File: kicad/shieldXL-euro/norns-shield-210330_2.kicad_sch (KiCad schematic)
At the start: 48 parts, among them J1 PJ-320B, J2 PJ-320B, SW1 PVA1, SW2 PVA1, SW3 PVA1, U5 HCPL-0631-500E

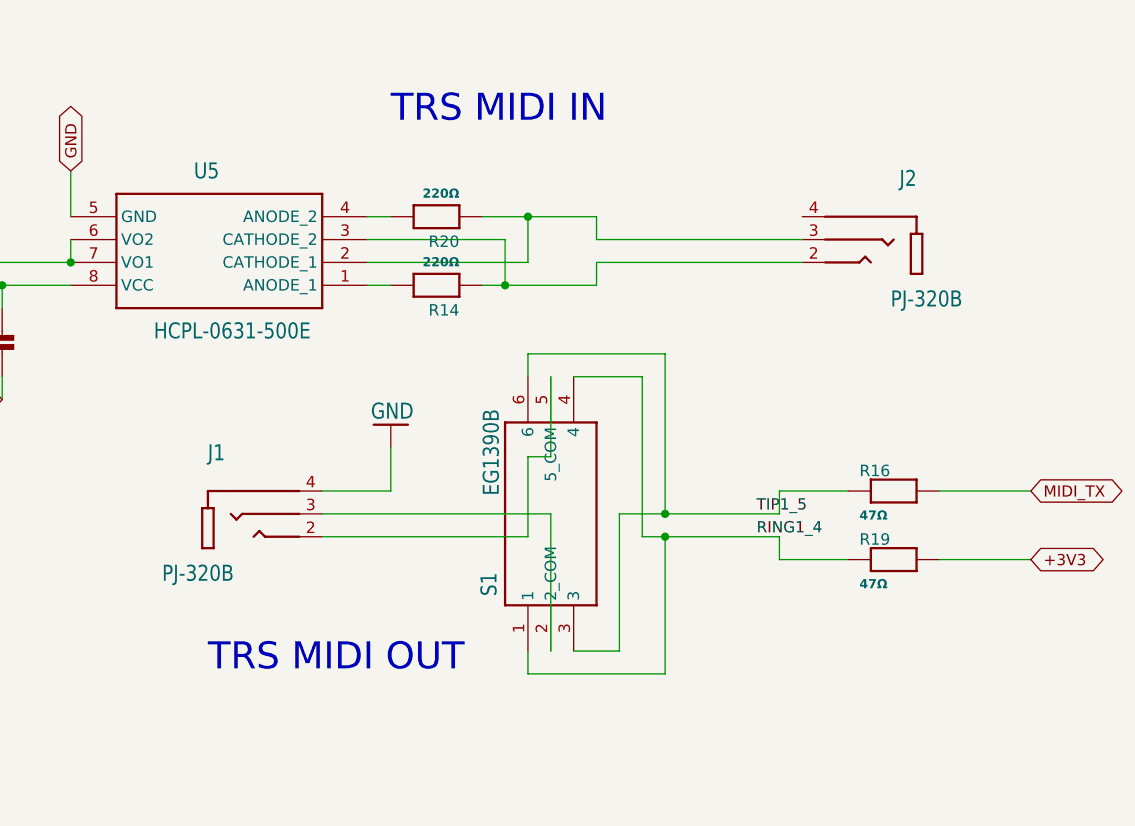
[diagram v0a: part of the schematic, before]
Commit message: Remove the desktop I/O: 6.35 mm jacks, PJ-320B MIDI jacks, A/B slide switch
tools/strip_shield_io.py takes J1, J2, J4, J5 off sheet 1 and J3, J6, S1 off
sheet 2, puts a global label wherever a signal reached them (IN_L_LINE,
IN_R_LINE, OUT_L_LINE, OUT_R_LINE, MIDI_OUT_SRC, MIDI_OUT_SNK, MIDI_IN_TIP,
MIDI_IN_RING), and prunes the wires left hanging. Checked against the
baseline netlist: every net keeps exactly its connections, less the removed
parts' pins. The Eurorack I/O that replaces them comes next.

Co-Authored-By: Claude Opus 5.5 <noreply@anthropic.com>
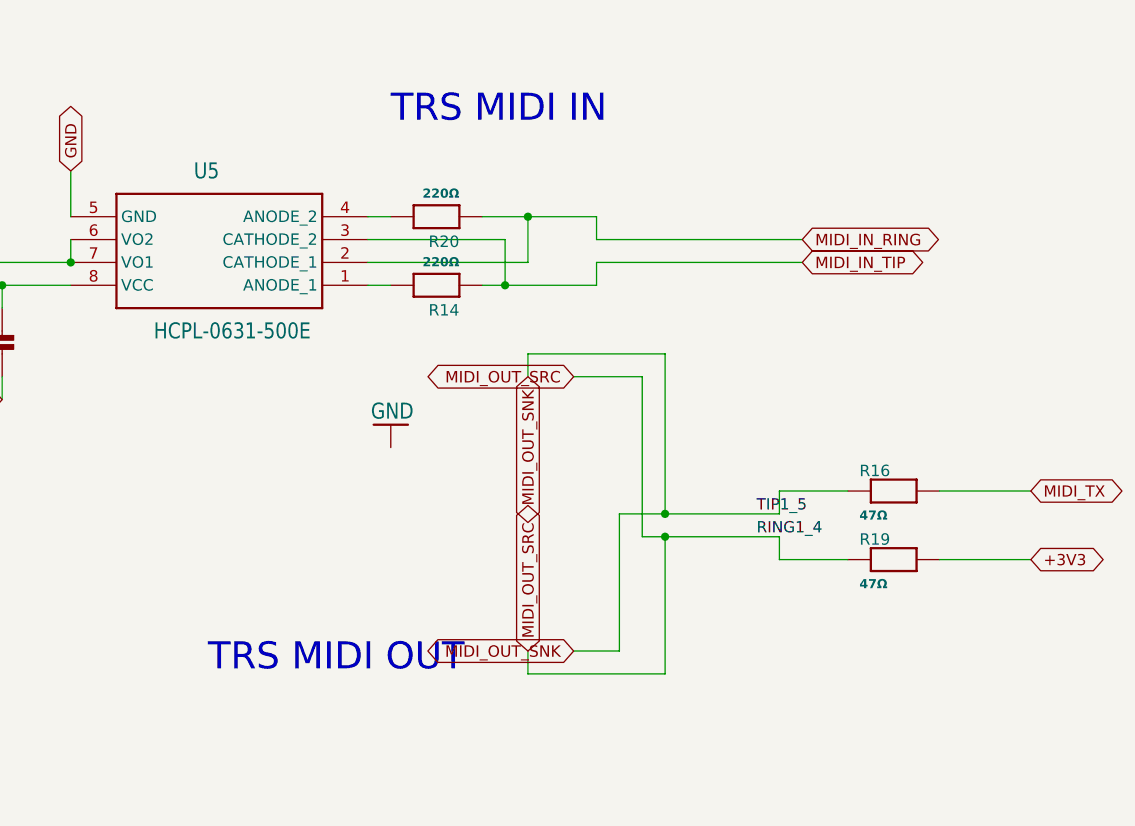
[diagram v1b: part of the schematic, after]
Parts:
- removed J1, J2: PJ-320B, ShieldXL:LUOYANG-DISHANG_PJ-320B, symbol Hachi-Ni_v26-eagle-import:PJ-320B
- removed S1: EG1390B, ShieldXL:SOP250P600X400-6N, symbol Hachi-Ni_v26-eagle-import:EG1390B
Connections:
- net MIDI_IN_RING: now reaches R20.1, U5.2 (CATHODE_1)
- net MIDI_IN_TIP: now reaches R14.1, U5.3 (CATHODE_2)
- net RING1_4 renamed MIDI_OUT_SRC
- net TIP1_5 renamed MIDI_OUT_SNK

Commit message: Add the Eurorack I/O sheet and the MMM footprint library
tools/make_eurorack_sheet.py writes eurorack.kicad_sch and hooks it into the
root as page 3: 10-pin rack power (op-amps only), 3.5 mm audio in/out through
a TL074 scaling 10 Vpp to the codec and back, PJ366ST MIDI jacks with Type A/B
on solder jumpers, USB-C power for the Pi through a polyfuse and TVS, and three
panel USB-A sockets cabled to the Pi. It joins the shield sheets by the global
labels the strip step placed.

strip_shield_io.py also removes the ground symbols left pinned to nothing once
the jacks were gone, in the same run as the strip. MMM.pretty and its 3D models
come from the Missing Mile Modular library; README.md covers the conversion,
the levels and what is left. Stop tracking __pycache__.

Co-Authored-By: Claude Opus 5.5 <noreply@anthropic.com>
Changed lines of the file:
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@@
-	)
-	(symbol
-		(lib_id "Hachi-Ni_v26-eagle-import:supply1_GND")
-		(at 196.85 53.594 180)
-		(unit 1)
-		(exclude_from_sim no)
-		(in_bom yes)
-		(on_board yes)
-		(dnp no)
-		(property "Reference" "#GND3"
-			(at 196.85 53.594 0)
-			(effects
-				(font
-					(size 1.27 1.27)
-				)
-				(hide yes)
-			)
-		)
-		(property "Value" "GND"
-			(at 199.39 51.054 0)
-			(effects
-				(font
-					(size 1.778 1.5113)
-				)
-				(justify left bottom)
-			)
-		)
-		(property "Footprint" ""
-			(at 196.85 53.594 0)
-			(effects
-				(font
-					(size 1.27 1.27)
-				)
-				(hide yes)
-			)
-		)
-		(property "Datasheet" ""
-			(at 196.85 53.594 0)
-			(effects
-				(font
-					(size 1.27 1.27)
-				)
-				(hide yes)
-			)
-		)
-		(property "Description" ""
-			(at 196.85 53.594 0)
-			(effects
-				(font
-					(size 1.27 1.27)
-				)
-				(hide yes)
-			)
-		)
-		(pin "1"
-		)
-		(instances
-			(project "Hachi-Ni_v26"
-				(path "/62ca0448-8214-4fa6-89ca-4a62b295d057/dcf1a22e-2574-4c83-a4dc-208deeeb6342"
-					(reference "#GND3")
-					(unit 1)
-				)
-			)
-			(project "shieldXL-euro"
-				(path "/b86e8947-58dc-49c6-bb5d-ce6d33c2e465/53fda09e-7af9-4285-ac8e-05ed312a27ba"
-					(reference "#GND06")
-					(unit 1)
-				)
-			)
-		)
 	)
 	(symbol

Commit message: Keys: C&K D6R00 round key switches for K1-K3
Footprint from the ITT Cannon D6 datasheet (D-18): four 0.8 mm PC pins on a
5.0 mm square, body d12.0, cap d9.0. The datasheet does not say which pins
pair inside, so SW1 and SW2 take opposite corners, on different contacts
either way; the other two pins hold the switch. Replaces shieldXL's
Choc/MX footprint, too wide for the 13.6 mm between K2 and K3.

Co-Authored-By: Claude Opus 5.5 <noreply@anthropic.com>
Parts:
- SW1, SW2, SW3: value PVA1 -> D6R00 F1 LFS; footprint ShieldXL:Choc_MX_combo -> MMM:SW_CK_D6R
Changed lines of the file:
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@@
 			)
 		)
-		(property "Value" "PVA1"
+		(property "Value" "D6R00 F1 LFS"
 			(at 240.03 198.12 0)
 			(effects
@@
 			)
 		)
-		(property "Footprint" "ShieldXL:Choc_MX_combo"
+		(property "Footprint" "MMM:SW_CK_D6R"
 			(at 243.84 196.85 0)
 			(effects
@@
 			)
 		)
-		(property "Value" "PVA1"
+		(property "Value" "D6R00 F1 LFS"
 			(at 240.03 165.1 0)
 			(effects
@@
 			)
 		)
-		(property "Footprint" "ShieldXL:Choc_MX_combo"
+		(property "Footprint" "MMM:SW_CK_D6R"
 			(at 243.84 163.83 0)
 			(effects
@@
 			)
 		)
-		(property "Value" "PVA1"
+		(property "Value" "D6R00 F1 LFS"
 			(at 240.03 129.54 0)
 			(effects
@@
 			)
 		)
-		(property "Footprint" "ShieldXL:Choc_MX_combo"
+		(property "Footprint" "MMM:SW_CK_D6R"
 			(at 243.84 128.27 0)
 			(effects

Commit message: Board: K1-K3 on the D6R footprint; keys are populated
shieldXL left its keys unfitted (DNP) for builders to choose; Moirae fits
the D6R00.

Co-Authored-By: Claude Opus 5.5 <noreply@anthropic.com>
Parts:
- SW1, SW2, SW3: now fitted
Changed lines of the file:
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@@
 		(in_bom yes)
 		(on_board yes)
-		(dnp yes)
+		(dnp no)
 		(property "Reference" "SW3"
 			(at 240.03 186.69 0)
@@
 		(in_bom yes)
 		(on_board yes)
-		(dnp yes)
+		(dnp no)
 		(property "Reference" "SW2"
 			(at 240.03 153.67 0)
@@
 		(in_bom yes)
 		(on_board yes)
-		(dnp yes)
+		(dnp no)
 		(property "Reference" "SW1"
 			(at 240.03 118.11 0)

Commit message: 3D models for shieldXL's parts; encoders populated
tools/set_3d_models.py gives the Eagle-imported footprints KiCad's stock
models, turned to match their pads (found by matching pad positions; KiCad
turns a model the opposite way to a footprint, checked on U1's pin 1), points
the encoders at the repo's PEC11R model instead of a missing Mac path, fixes
U2's KiCad 6 path, and stands the 1812 resistor model in for the fuse. Q1
takes the XO53 oscillator body (5.0 x 3.2, as the ASFL1).

E1-E3 were do-not-populate from shieldXL, which hid them in 3D; Moirae fits
them.

Co-Authored-By: Claude Opus 5.5 <noreply@anthropic.com>
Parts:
- E1, E2, E3: now fitted
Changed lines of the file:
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@@
 		(in_bom yes)
 		(on_board yes)
-		(dnp yes)
+		(dnp no)
 		(property "Reference" "E1"
 			(at 101.6 127 0)
@@
 		(in_bom yes)
 		(on_board yes)
-		(dnp yes)
+		(dnp no)
 		(property "Reference" "E2"
 			(at 101.6 177.8 0)
@@
 		(in_bom yes)
 		(on_board yes)
-		(dnp yes)
+		(dnp no)
 		(property "Reference" "E3"
 			(at 101.6 228.6 0)

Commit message: Circuit review: USB ESD and bulk, MIDI out buffer, panel MIDI LEDs, non-inverting inputs, display decoupling, AGND-GND jumper
- U102-U104 USBLC6-2SC6 on each panel USB-A's D+/D-, with 47u + 100n on
  its VBUS (C114-C119): the ports are on the panel, the Pi 10 cm away.
- U105 74LVC1G125 between the Pi's TXD and the MIDI out resistor and TX LED
  (MIDI_TX -> MIDI_TX_BUF): a TRS plug going in shorts tip/ring to sleeve,
  and the buffer takes that, not the Pi. R17 47 -> 100 ohm keeps that
  short under the buffer's 50 mA and the loop at about 5 mA.
- D1 / D2 come out to the panel: red 3 mm LEDs (MMM:LED_3mm_PadsAC, pads
  named A/C for shieldXL's symbol) between the MIDI jacks, 470 ohm each.
- Inputs: 69.8k / 30.1k divider into a follower instead of the inverting
  stage, so audio keeps its polarity; 13.4 Vpp reaches codec full scale.
- C121 / C122 10u + 100n on +3V3 at the display's FPC connector.
- JP103, open, across the AGND-GND ferrite L3.

Co-Authored-By: Claude Opus 5.5 <noreply@anthropic.com>
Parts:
- D6: value RED -> RED 3mm; footprint ShieldXL:CHIPLED_0603_NOOUTLINE -> MMM:LED_3mm_PadsAC
- D7: value BLUE -> RED 3mm; footprint ShieldXL:CHIPLED_0603_NOOUTLINE -> MMM:LED_3mm_PadsAC
- R16: value 47Ω -> 100Ω
- R21: value 47Ω -> 470Ω
- R22: value 15Ω -> 470Ω
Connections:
- net MIDI_TX renamed MIDI_TX_BUF
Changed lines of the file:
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@@
 		)
 	)
-	(global_label "MIDI_TX"
+	(global_label "MIDI_TX_BUF"
 		(shape bidirectional)
 		(at 334.01 48.26 0)
@@
 		)
 	)
-	(global_label "MIDI_TX"
+	(global_label "MIDI_TX_BUF"
 		(shape bidirectional)
 		(at 267.97 60.96 0)
@@
 			)
 		)
-		(property "Value" "47Ω"
+		(property "Value" "470Ω"
 			(at 303.53 33.02 0)
 			(effects
@@
 			)
 		)
-		(property "Value" "BLUE"
+		(property "Value" "RED 3mm"
 			(at 330.2 43.434 0)
 			(effects
@@
 			)
 		)
-		(property "Footprint" "ShieldXL:CHIPLED_0603_NOOUTLINE"
+		(property "Footprint" "MMM:LED_3mm_PadsAC"
 			(at 331.47 40.64 0)
 			(effects
@@
 			)
 		)
-		(property "Value" "RED"
+		(property "Value" "RED 3mm"
 			(at 307.34 43.434 0)
 			(effects
@@
 			)
 		)
-		(property "Footprint" "ShieldXL:CHIPLED_0603_NOOUTLINE"
+		(property "Footprint" "MMM:LED_3mm_PadsAC"
 			(at 308.61 40.64 0)
 			(effects
@@
 			)
 		)
-		(property "Value" "47Ω"
+		(property "Value" "100Ω"
 			(at 248.92 64.262 0)
 			(effects
@@
 			)
 		)
-		(property "Value" "15Ω"
+		(property "Value" "470Ω"
 			(at 326.39 33.02 0)
 			(effects
